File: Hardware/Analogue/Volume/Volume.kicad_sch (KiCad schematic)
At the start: 20 parts, among them J1 Audio In Right, J10 Buffer Out Right, J11 Buffer Out Left, J2 Audio In Left, J3 Audio Power, J4 Digital Power, J5 Audio In Left, J6 Audio In Right, J7 Buffer Power, J8 Buffer In Left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

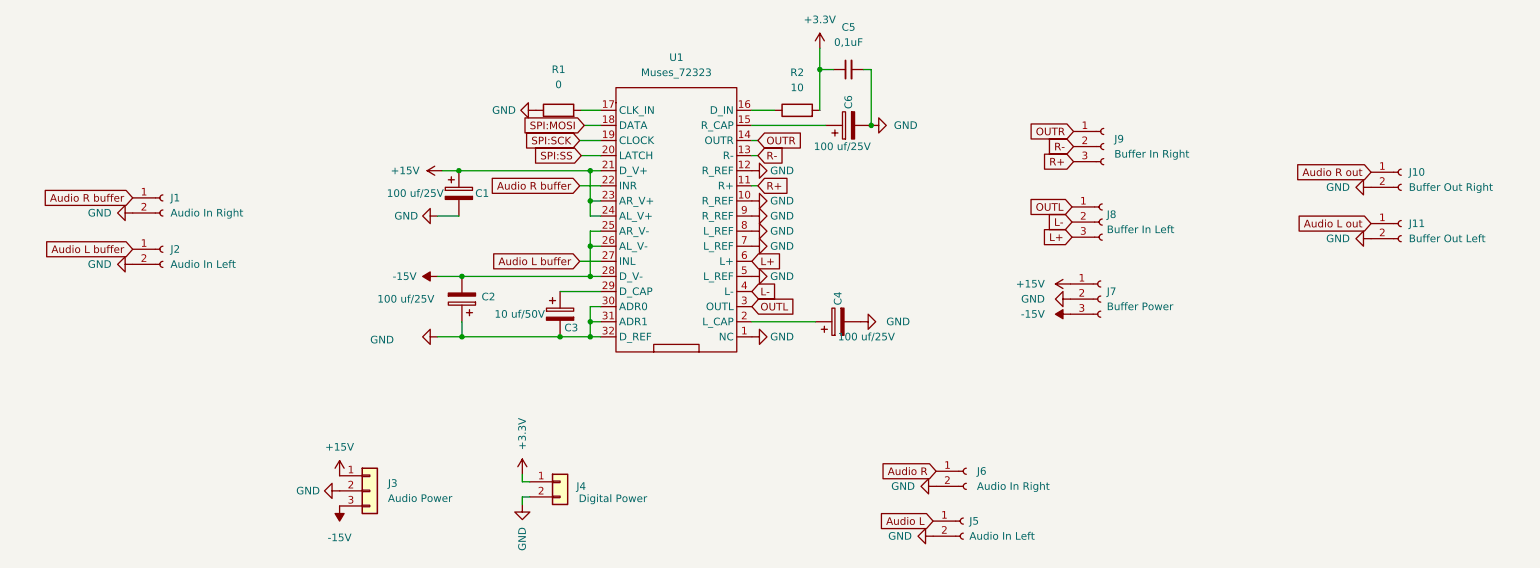
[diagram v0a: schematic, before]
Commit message: Separating digital and analog ground
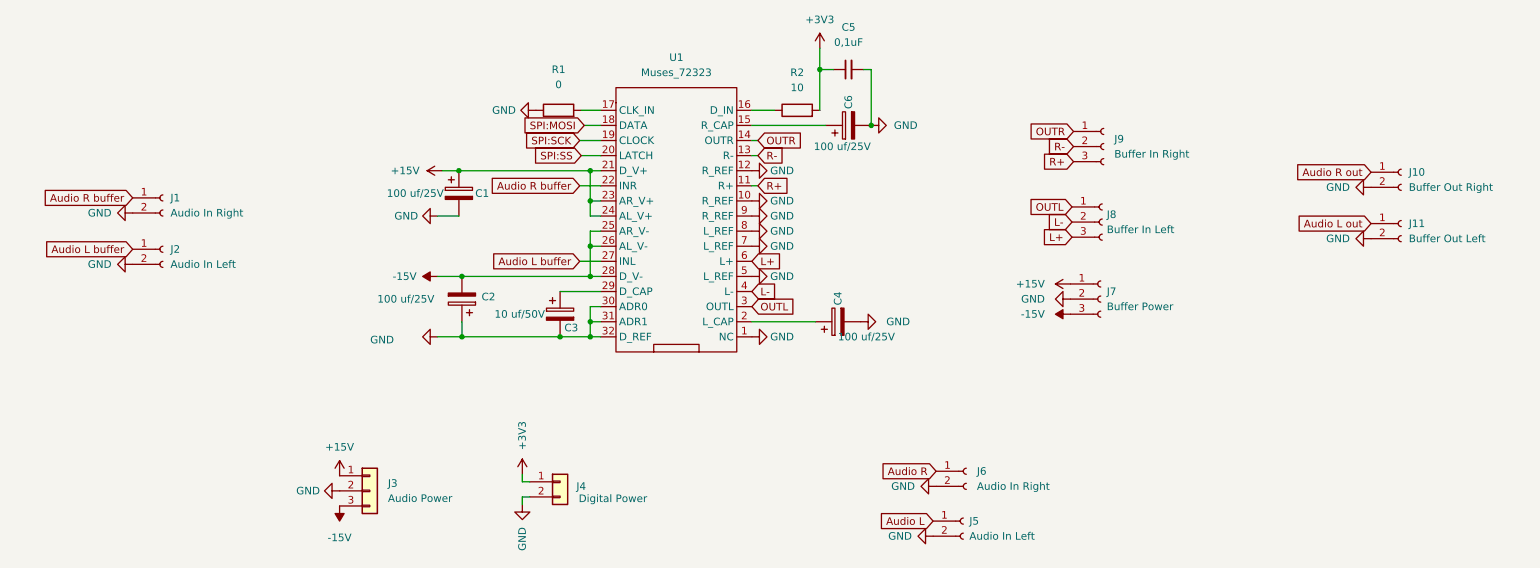
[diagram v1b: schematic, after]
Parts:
- J9: value Buffer In Right -> Buffer In Right
